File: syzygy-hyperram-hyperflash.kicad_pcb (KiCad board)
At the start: 4 copper layers, 0 parts

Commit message: Added PCB template for STD-SYZYGY
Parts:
- added FID5: Fiducial, Fiducial:Fiducial_1mm_Mask2mm, F.Cu at (103.9, 65.2)
- added FID6: Fiducial, Fiducial:Fiducial_1mm_Mask2mm, F.Cu at (144.6, 55.3)
- added FID7: Fiducial, Fiducial:Fiducial_1mm_Mask2mm, F.Cu at (103.0, 121.9)
- added FID8: Fiducial, Fiducial:Fiducial_1mm_Mask2mm, F.Cu at (144.9, 121.7)
- added G***: LOGO, SYZYGY:SYZYGY_Logo, F.Cu at (123.6, 56.7)
- added H1: MountingHole_Pad, SYZYGY:MountingHole_3.2mm_M3_6.5mm_Pad_TopBottom, F.Cu at (107.1, 60.3)
- added H2: MountingHole_Pad, SYZYGY:MountingHole_3.2mm_M3_6.5mm_Pad_TopBottom, F.Cu at (141.1, 60.3)
- added H3: MountingHole_Pad, SYZYGY:MountingHole_3.2mm_M3_6.5mm_Pad_TopBottom, F.Cu at (106.6, 70.3)
- added H4: MountingHole_Pad, SYZYGY:MountingHole_3.2mm_M3_6.5mm_Pad_TopBottom, F.Cu at (141.6, 70.3)
- added H5: MountingHole_Pad, SYZYGY:MountingHole_3.2mm_M3_6.5mm_Pad_TopBottom, F.Cu at (106.6, 118.3)
- added H6: MountingHole_Pad, SYZYGY:MountingHole_3.2mm_M3_6.5mm_Pad_TopBottom, F.Cu at (141.6, 118.3)
- added J1: SYZYGY_STD, SYZYGY:QTE-020-01-F-D-A, B.Cu at (124.1, 60.3)
- added REF**: SYZYGY_STD_Logo, SYZYGY:SYZYGY_STD_Logo, F.Cu at (110.2, 56.5)
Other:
- board outline added: 45 x 70 mm

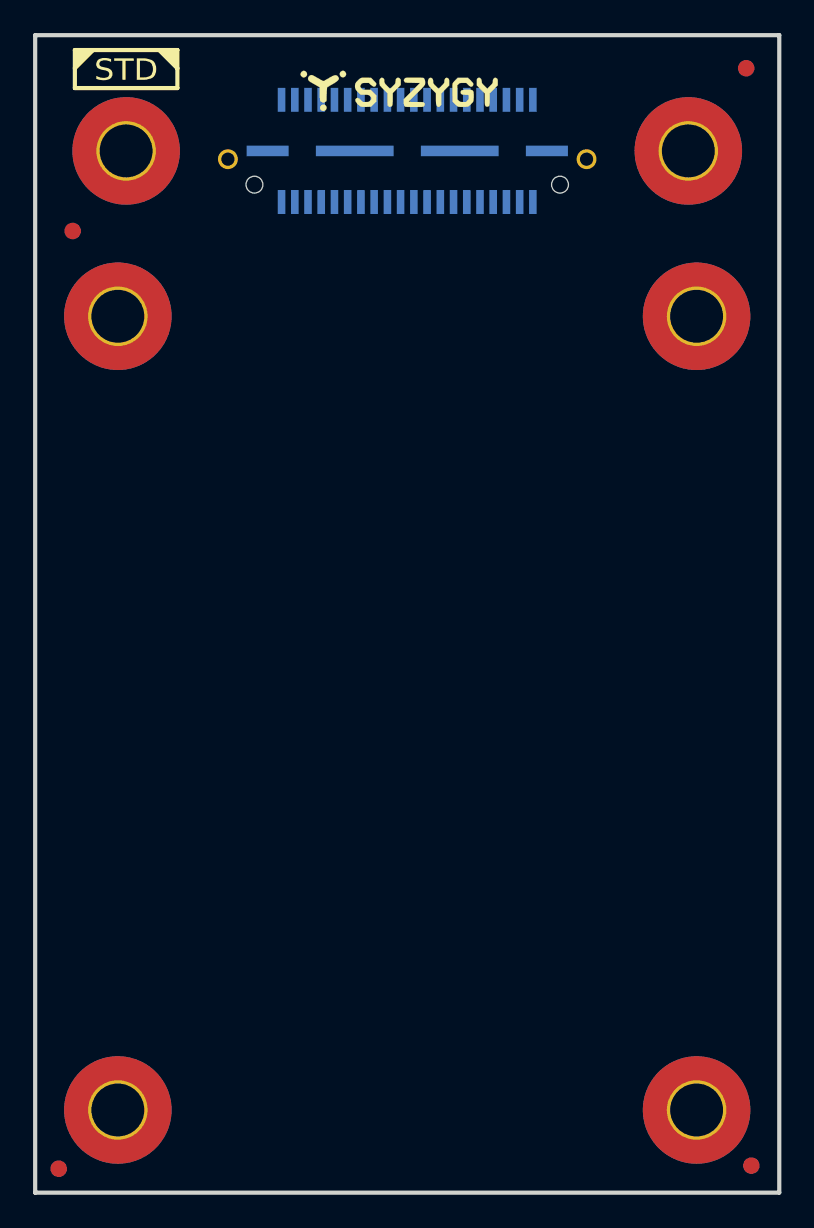
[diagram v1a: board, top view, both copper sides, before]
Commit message: Updated PCB after latest changes in schematic
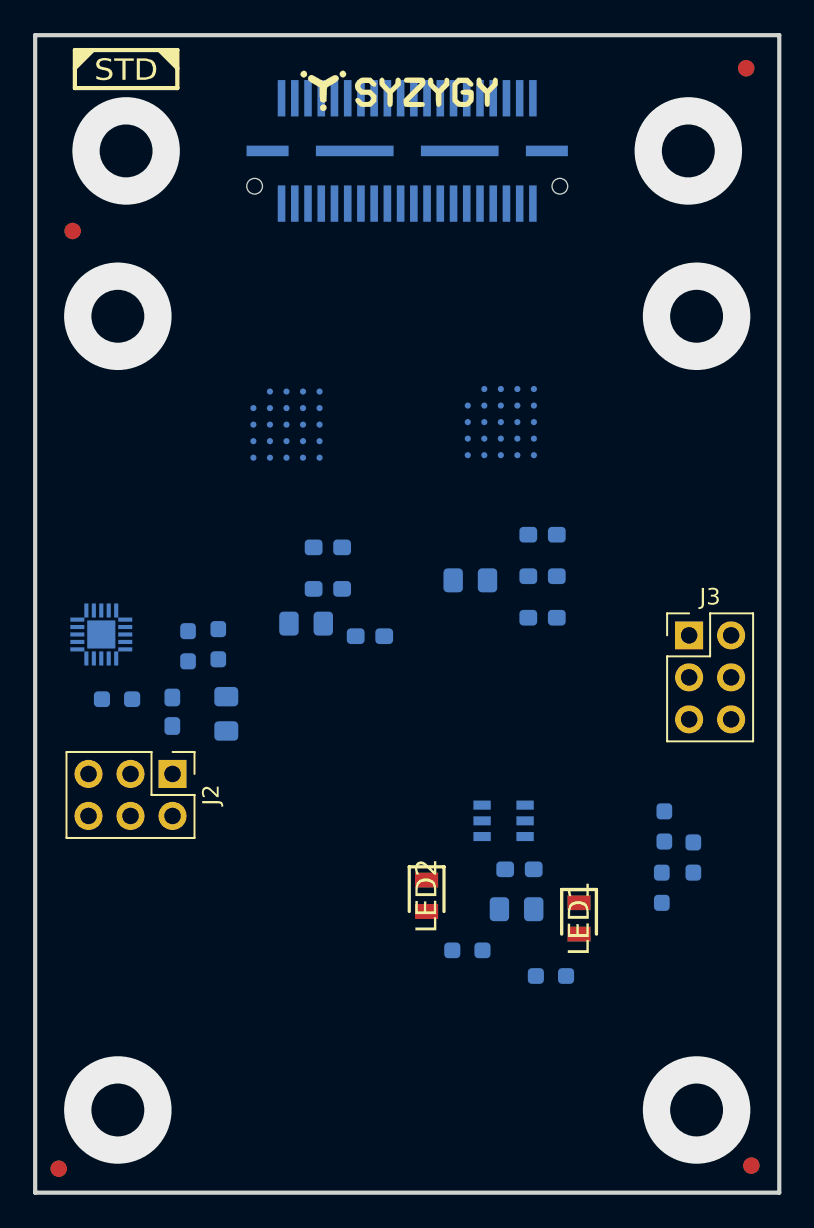
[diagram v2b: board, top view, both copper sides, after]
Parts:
- removed H1, H2, H3, H4, H5, H6: MountingHole_Pad, SYZYGY:MountingHole_3.2mm_M3_6.5mm_Pad_TopBottom
- added C1: 100nF, Capacitor_SMD:C_0603_1608Metric_Pad1.08x0.95mm_HandSolder, B.Cu at (109.9, 94.2)
- added C10: 100n, Capacitor_SMD:C_0603_1608Metric_Pad1.08x0.95mm_HandSolder, B.Cu at (121.9, 89.7)
- added C11: 100n, Capacitor_SMD:C_0603_1608Metric_Pad1.08x0.95mm_HandSolder, B.Cu at (119.3, 84.3)
- added C12: 100n, Capacitor_SMD:C_0603_1608Metric_Pad1.08x0.95mm_HandSolder, B.Cu at (119.3, 86.8)
- added C2: 1uF, Capacitor_SMD:C_0805_2012Metric_Pad1.18x1.45mm_HandSolder, B.Cu at (113.2, 94.4)
- added C3: 1uF, Capacitor_SMD:C_0805_2012Metric_Pad1.18x1.45mm_HandSolder, B.Cu at (130.7, 106.2)
- added C4: 100nF, Capacitor_SMD:C_0603_1608Metric_Pad1.08x0.95mm_HandSolder, B.Cu at (130.9, 103.8)
- added C5: 1u 16v, Capacitor_SMD:C_0805_2012Metric_Pad1.18x1.45mm_HandSolder, B.Cu at (127.9, 86.3)
- added C6: 100n, Capacitor_SMD:C_0603_1608Metric_Pad1.08x0.95mm_HandSolder, B.Cu at (132.3, 83.5)
- added C7: 100n, Capacitor_SMD:C_0603_1608Metric_Pad1.08x0.95mm_HandSolder, B.Cu at (132.3, 86.0)
- added C8: 100n, Capacitor_SMD:C_0603_1608Metric_Pad1.08x0.95mm_HandSolder, B.Cu at (132.3, 88.5)
- added C9: 1u 16v, Capacitor_SMD:C_0805_2012Metric_Pad1.18x1.45mm_HandSolder, B.Cu at (118.0, 88.9)
- added IC1: ATTINY44A-MMH, syzygy-hyperram-hyperflash:QFN45P300X300X85-21N, B.Cu at (105.6, 89.6)
- added IC2: TLV6710DDCT, syzygy-hyperram-hyperflash:SOT95P280X100-6N, B.Cu at (130.0, 100.8)
- added IC3: S27KL0641DABHI020, syzygy-hyperram-hyperflash:BGA24C100P5X5_600X800X100, B.Cu at (129.8, 76.7)
- added IC4: S71KL256SC0BHI, syzygy-hyperram-hyperflash:BGA24C100P5X5_600X800X100, B.Cu at (116.8, 76.9)
- added J2: Conn_02x03_Odd_Even, Connector_PinHeader_2.54mm:PinHeader_2x03_P2.54mm_Vertical, F.Cu at (109.9, 98.0)
- added J3: Conn_02x03_Odd_Even, Connector_PinHeader_2.54mm:PinHeader_2x03_P2.54mm_Vertical, F.Cu at (141.2, 89.6)
- added LED1: 150080VS75000, syzygy-hyperram-hyperflash:LEDC2012X80N, F.Cu at (134.5, 106.7)
- added LED2: 150080VS75000, syzygy-hyperram-hyperflash:LEDC2012X80N, F.Cu at (125.3, 105.4)
- added R1: 10k, Resistor_SMD:R_0603_1608Metric_Pad0.98x0.95mm_HandSolder, B.Cu at (106.6, 93.5)
- added R2: 220, Resistor_SMD:R_0603_1608Metric_Pad0.98x0.95mm_HandSolder, B.Cu at (132.8, 110.2)
- added R3: 220, Resistor_SMD:R_0603_1608Metric_Pad0.98x0.95mm_HandSolder, B.Cu at (127.8, 108.7)
- added R4: 287k, Resistor_SMD:R_0603_1608Metric_Pad0.98x0.95mm_HandSolder, B.Cu at (139.7, 101.2)
- added R5: 4k, Resistor_SMD:R_0603_1608Metric_Pad0.98x0.95mm_HandSolder, B.Cu at (141.4, 103.0)
- added R6: 40k, Resistor_SMD:R_0603_1608Metric_Pad0.98x0.95mm_HandSolder, B.Cu at (139.5, 104.9)
- added R7: 10k, Resistor_SMD:R_0603_1608Metric_Pad0.98x0.95mm_HandSolder, B.Cu at (110.9, 90.3)
- added R8: 10k, Resistor_SMD:R_0603_1608Metric_Pad0.98x0.95mm_HandSolder, B.Cu at (112.7, 90.1)
- J1: footprint SYZYGY:QTE-020-01-F-D-A -> syzygy-hyperram-hyperflash:QTE-020-XX-YYY-D-A
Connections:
- J1 pad 0: (no net) -> GND
- J1 pad 1: (no net) -> /SCK
- J1 pad 10: (no net) -> /HF_DQ2
- J1 pad 11: (no net) -> /HF_CS2N
- J1 pad 12: (no net) -> /HF_DQ5
- J1 pad 13: (no net) -> /HF_CLK+
- J1 pad 14: (no net) -> /HF_DQ0
- J1 pad 15: (no net) -> /HF_CLK-
- J1 pad 16: (no net) -> /HF_DQ6
- J1 pad 17: (no net) -> unconnected-(J1-S12_D6P-Pad17)
- J1 pad 18: (no net) -> /HF_DQ7
- J1 pad 19: (no net) -> /HR_DQ4
- J1 pad 2: (no net) -> +5V
- J1 pad 20: (no net) -> /HF_DQ1
- J1 pad 21: (no net) -> /HR_DQ3
- J1 pad 22: (no net) -> /HF_RWDS
- J1 pad 23: (no net) -> /HR_DQ2
- J1 pad 24: (no net) -> /HF_RSTON
- J1 pad 25: (no net) -> /HR_DQ5
- J1 pad 26: (no net) -> /HF_INTN
- J1 pad 27: (no net) -> /HR_DQ0
- J1 pad 28: (no net) -> /HF_RSTN
- J1 pad 29: (no net) -> /HR_DQ6
- J1 pad 3: (no net) -> /SDA_MOSI
- J1 pad 30: (no net) -> /HR_CSN
- J1 pad 31: (no net) -> /HR_DQ7
- J1 pad 32: (no net) -> /HR_RSTN
- J1 pad 33: (no net) -> /HR_DQ1
- J1 pad 34: (no net) -> /HR_CLK+
- J1 pad 35: (no net) -> /HR_RWDS
- J1 pad 36: (no net) -> /HR_CLK-
- J1 pad 37: (no net) -> unconnected-(J1-RSVD-Pad37)
- J1 pad 38: (no net) -> unconnected-(J1-RSVD-Pad38)
- J1 pad 39: (no net) -> VCC
- J1 pad 4: (no net) -> /RGA
- J1 pad 40: (no net) -> +3.3V
- J1 pad 5: (no net) -> /HF_PSC+
- J1 pad 6: (no net) -> /HF_DQ4
- J1 pad 7: (no net) -> /HF_PSC-
- J1 pad 8: (no net) -> /HF_DQ3
- J1 pad 9: (no net) -> /HF_CSN
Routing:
- net (no net): vias 0 -> 6

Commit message: Routed all signals to HyperRAM (IC3)
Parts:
- C5, C6, C7, C8: moved to F.Cu
- moved C5 12.8 mm to (139.5, 80.6), turned to 0 degrees
- moved C8 10.8 mm to (128.7, 78.4)
- moved C7 5.87 mm to (127.5, 82.6), turned to 0 degrees
- moved IC4 4.35 mm to (113.8, 80.0)
- moved IC3 3.65 mm to (128.2, 80.0)
- moved C6 2.99 mm to (129.9, 81.7), turned to -90 degrees
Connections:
- J1 pad 10: /HF_DQ2 -> /HF_DQ1
- J1 pad 12: /HF_DQ5 -> /HF_DQ6
- J1 pad 16: /HF_DQ6 -> /HF_DQ5
- J1 pad 17: unconnected-(J1-S12_D6P-Pad17) -> /HR_CSN
- J1 pad 18: /HF_DQ7 -> /HF_DQ2
- J1 pad 19: /HR_DQ4 -> /HR_RWDS
- J1 pad 20: /HF_DQ1 -> /HF_DQ3
- J1 pad 21: /HR_DQ3 -> /HR_DQ7
- J1 pad 22: /HF_RWDS -> /HF_DQ4
- J1 pad 23: /HR_DQ2 -> /HR_DQ1
- J1 pad 25: /HR_DQ5 -> /HR_DQ6
- J1 pad 29: /HR_DQ6 -> /HR_DQ5
- J1 pad 30: /HR_CSN -> unconnected-(J1-S25-Pad30)
- J1 pad 31: /HR_DQ7 -> /HR_DQ2
- J1 pad 33: /HR_DQ1 -> /HR_DQ3
- J1 pad 35: /HR_RWDS -> /HR_DQ4
- J1 pad 6: /HF_DQ4 -> /HF_RWDS
- J1 pad 8: /HF_DQ3 -> /HF_DQ7
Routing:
- net /HR_DQ4: track 0.00 -> 28.0 mm
- net /HR_DQ3: track 0.00 -> 27.9 mm
- net /HR_DQ2: track 0.00 -> 27.9 mm
- net /HR_RWDS: track 0.00 -> 27.8 mm
- net /HR_DQ7: track 0.00 -> 27.8 mm
- net /HR_DQ6: track 0.00 -> 27.8 mm
- net /HR_DQ5: track 0.00 -> 27.8 mm
- net /HR_DQ1: track 0.00 -> 27.7 mm
- net /HR_CSN: track 0.00 -> 27.7 mm
- net /HR_DQ0: track 0.00 -> 27.7 mm
- net /HR_RSTN: track 0.00 -> 27.1 mm, vias 0 -> 2
- net /HR_CLK+: track 0.00 -> 25.0 mm, vias 0 -> 2
- net /HR_CLK-: track 0.00 -> 25.0 mm, vias 0 -> 2
- net GND: track 0.00 -> 4.34 mm, vias 0 -> 16
- net VCC: track 0.00 -> 3.86 mm, vias 0 -> 6

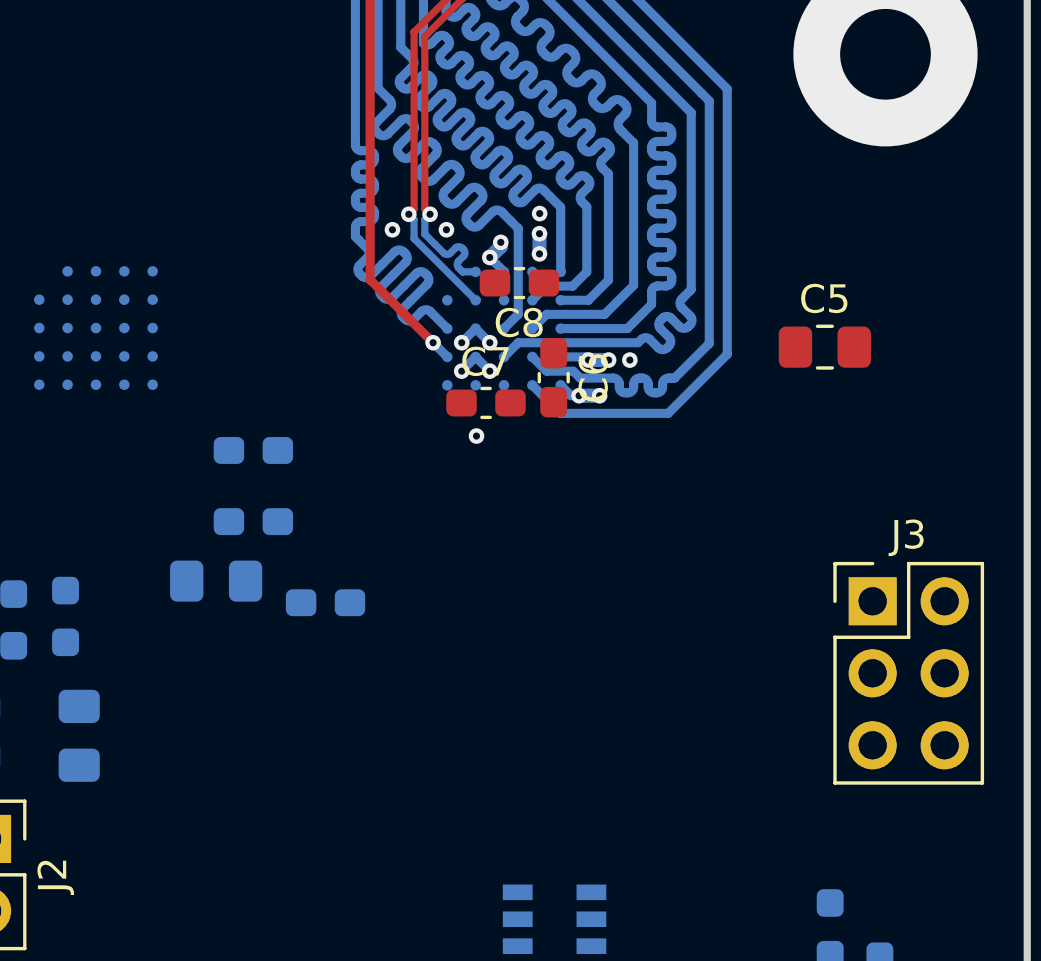
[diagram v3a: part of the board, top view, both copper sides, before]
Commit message: Added more filtering capacitors for HyperRAM and HyperFLash supply
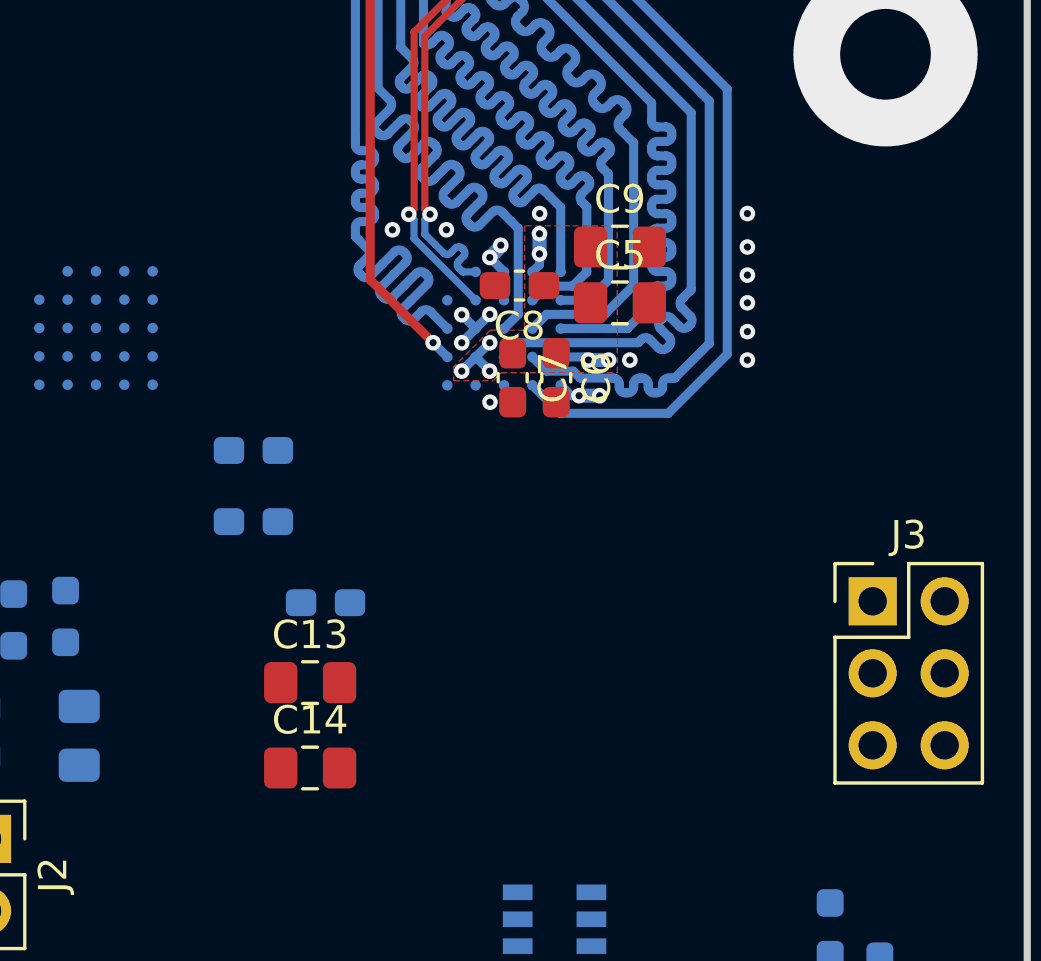
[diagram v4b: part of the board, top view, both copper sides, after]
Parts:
- added C13: 1u 16v, Capacitor_SMD:C_0805_2012Metric_Pad1.18x1.45mm_HandSolder, F.Cu at (121.3, 92.5)
- added C14: 1u 16v, Capacitor_SMD:C_0805_2012Metric_Pad1.18x1.45mm_HandSolder, F.Cu at (121.3, 95.5)
- C9: moved to F.Cu
- moved C9 18.5 mm to (132.3, 77.1), turned to 0 degrees
- moved C5 7.40 mm to (132.3, 79.1)
- moved C7 1.29 mm to (128.5, 81.7), turned to -90 degrees
- moved C6 0.09 mm to (130.0, 81.7)
- moved C8 0.09 mm to (128.7, 78.5)
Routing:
- net VCC: track 3.86 -> 5.30 mm, vias 6 -> 7
- net GND: track 4.34 -> 4.90 mm, vias 16 -> 23
- added copper zone on F.Cu, net VCC

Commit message: First, still not complete, try to route HyperFlash
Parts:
- C10, C11, C12: moved to F.Cu
- moved C10 15.4 mm to (114.9, 75.9)
- moved C11 7.61 mm to (112.5, 81.0), turned to 90 degrees
- moved C12 3.37 mm to (118.3, 83.6)
- moved IC4 1.09 mm to (114.9, 80.0)
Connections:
- J1 pad 10: /HF_DQ1 -> /HF_RSTN
- J1 pad 12: /HF_DQ6 -> /HF_RWDS
- J1 pad 14: /HF_DQ0 -> /HF_DQ7
- J1 pad 16: /HF_DQ5 -> /HF_DQ1
- J1 pad 18: /HF_DQ2 -> /HF_DQ6
- J1 pad 20: /HF_DQ3 -> /HF_DQ0
- J1 pad 22: /HF_DQ4 -> /HF_DQ5
- J1 pad 24: /HF_RSTON -> /HF_DQ3
- J1 pad 26: /HF_INTN -> /HF_DQ2
- J1 pad 28: /HF_RSTN -> /HF_DQ4
- J1 pad 6: /HF_RWDS -> /HF_RSTON
- J1 pad 8: /HF_DQ7 -> /HF_INTN
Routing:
- net /HF_CLK+: track 0.00 -> 31.4 mm
- net /HF_CLK-: track 0.00 -> 31.3 mm
- net /HF_DQ4: track 0.00 -> 30.2 mm, vias 0 -> 2
- net /HF_DQ2: track 0.00 -> 29.9 mm, vias 0 -> 2
- net /HF_DQ3: track 0.00 -> 27.9 mm, vias 0 -> 2
- net /HF_DQ0: track 0.00 -> 25.5 mm, vias 0 -> 2
- net /HF_DQ5: track 0.00 -> 25.5 mm, vias 0 -> 2
- net /SCK: track 0.00 -> 25.3 mm
- net /SDA_MOSI: track 0.00 -> 24.6 mm
- net /HF_RWDS: track 0.00 -> 23.6 mm, vias 0 -> 2
- net /HF_DQ1: track 0.00 -> 23.4 mm, vias 0 -> 2
- net /HF_DQ6: track 0.00 -> 23.3 mm, vias 0 -> 2
- net /HF_DQ7: track 0.00 -> 21.1 mm, vias 0 -> 2
- net /HF_PSC+: track 0.00 -> 20.4 mm, vias 0 -> 1
- net /HF_PSC-: track 0.00 -> 20.4 mm, vias 0 -> 1
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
